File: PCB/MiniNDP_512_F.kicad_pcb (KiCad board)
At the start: 2 copper layers, 60 x 34 mm, 19 parts, among them J1 Conn_02x20_Odd_Even, U1 HC238, U2 HC4040, U3 FCT841, U4 AS6C4008, U5 2G00

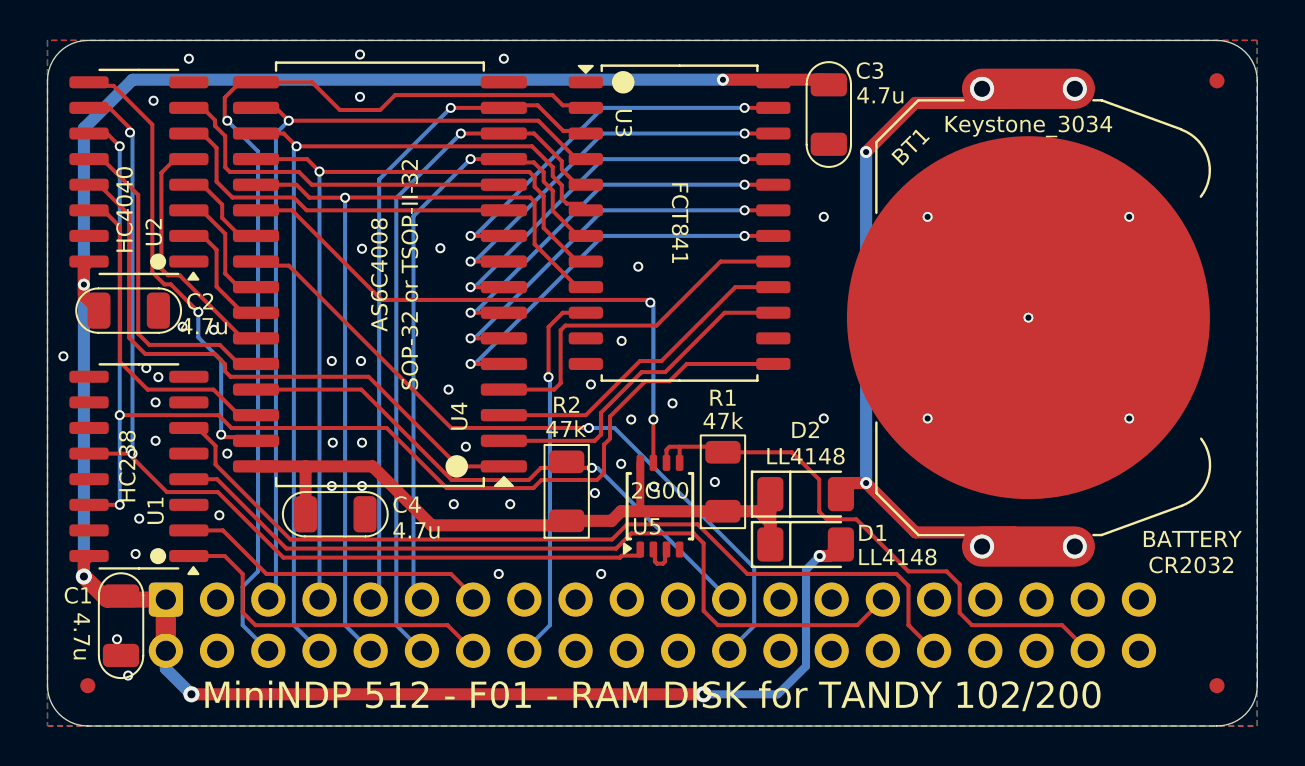
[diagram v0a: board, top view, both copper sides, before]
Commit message: replace 512_F with 512_G
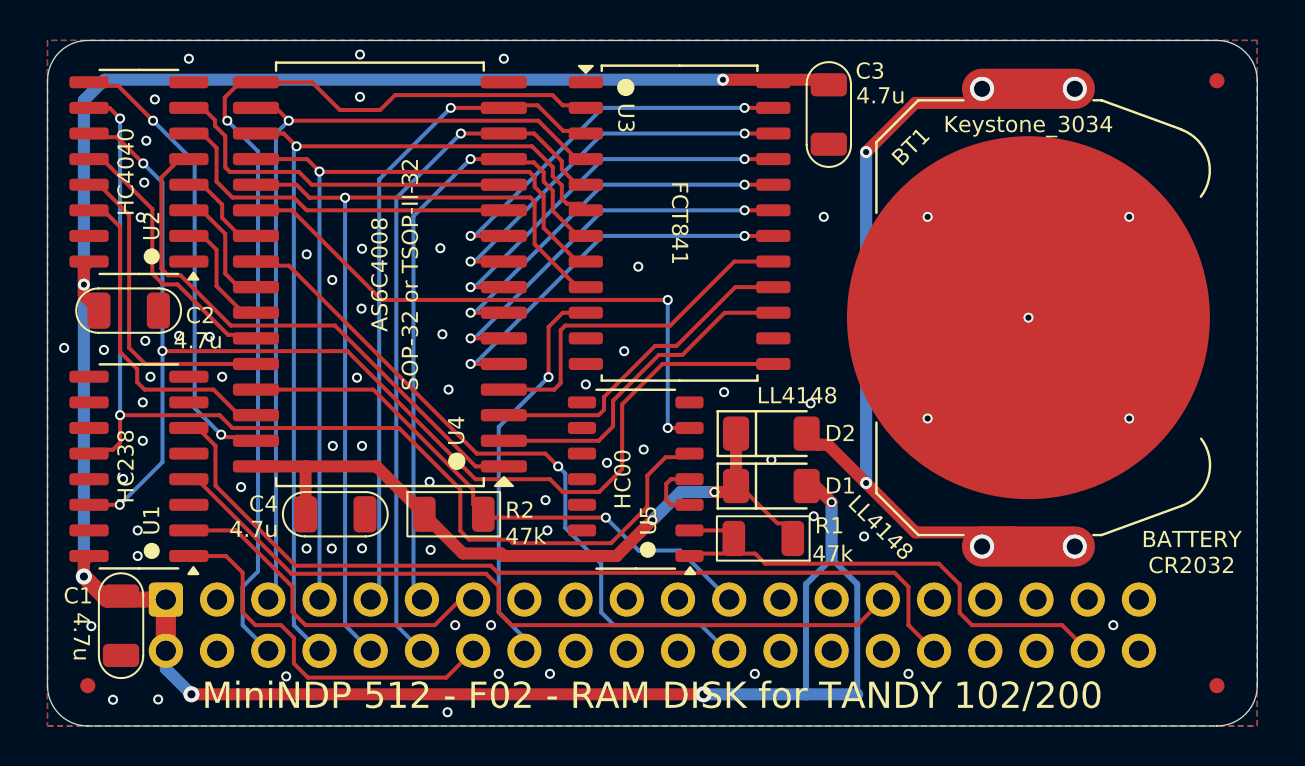
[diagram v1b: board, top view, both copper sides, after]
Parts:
- U5: value 2G00 -> HC00; footprint 000_LOCAL:TSSOP-8_3x3mm_P0.65mm -> 000_LOCAL:SOIC-14_3.9x8.7mm_P1.27mm
- moved R2 5.71 mm to (142.1, 109.5), turned to 0 degrees
- moved R1 3.45 mm to (157.4, 110.7), turned to 180 degrees
- moved D2 3.45 mm to (157.8, 105.5)
- moved D1 3.36 mm to (157.8, 108.1)
- moved U5 1.80 mm to (151.1, 107.8), turned to 180 degrees
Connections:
- U4 pad 1: /A7 -> /A3
- U4 pad 27: /A3 -> /A8
- U4 pad 28: /A8 -> /A7
- U5 pad 1: /BYTE -> /RAMRST
- U5 pad 2: Net-(U5-Pad2) -> /RAMRST
- U5 pad 3: Net-(U5-Pad2) -> Net-(U5-Pad3)
- U5 pad 4: GND -> Net-(U5-Pad3)
- U5 pad 5: /RAMRST -> /BYTE
- U5 pad 6: /RAMRST -> /~{CE}
- U5 pad 7: /~{CE} -> GND
- U5 pad 8: VMEM -> unconnected-(U5-Pad8)
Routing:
- net /A3: track 12.5 -> 27.3 mm
- net VBUS: track 112.1 -> 126.7 mm
- net /A7: track 30.1 -> 15.8 mm
- net /BYTE: track 48.6 -> 54.4 mm
- net Net-(U5-Pad3): track 0.00 -> 3.31 mm
- net /A8: track 16.5 -> 13.8 mm
- net /RAMRST: track 28.4 -> 25.7 mm
- net +BATT: track 36.6 -> 39.1 mm
- net /BUS_A8: track 17.2 -> 19.0 mm
- net Net-(U5-Pad2): track 1.84 -> 0.00 mm
- net /~{Y0}: track 40.5 -> 38.7 mm
- net /BLOCK: track 59.0 -> 60.7 mm
- net /BUS_A9: track 15.6 -> 17.3 mm
- net /~{RD}: track 35.6 -> 34.5 mm
- net /BUS_A10: track 18.8 -> 19.7 mm
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
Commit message: 512-F re-add ramrst diode, both-F remove /WR pullup
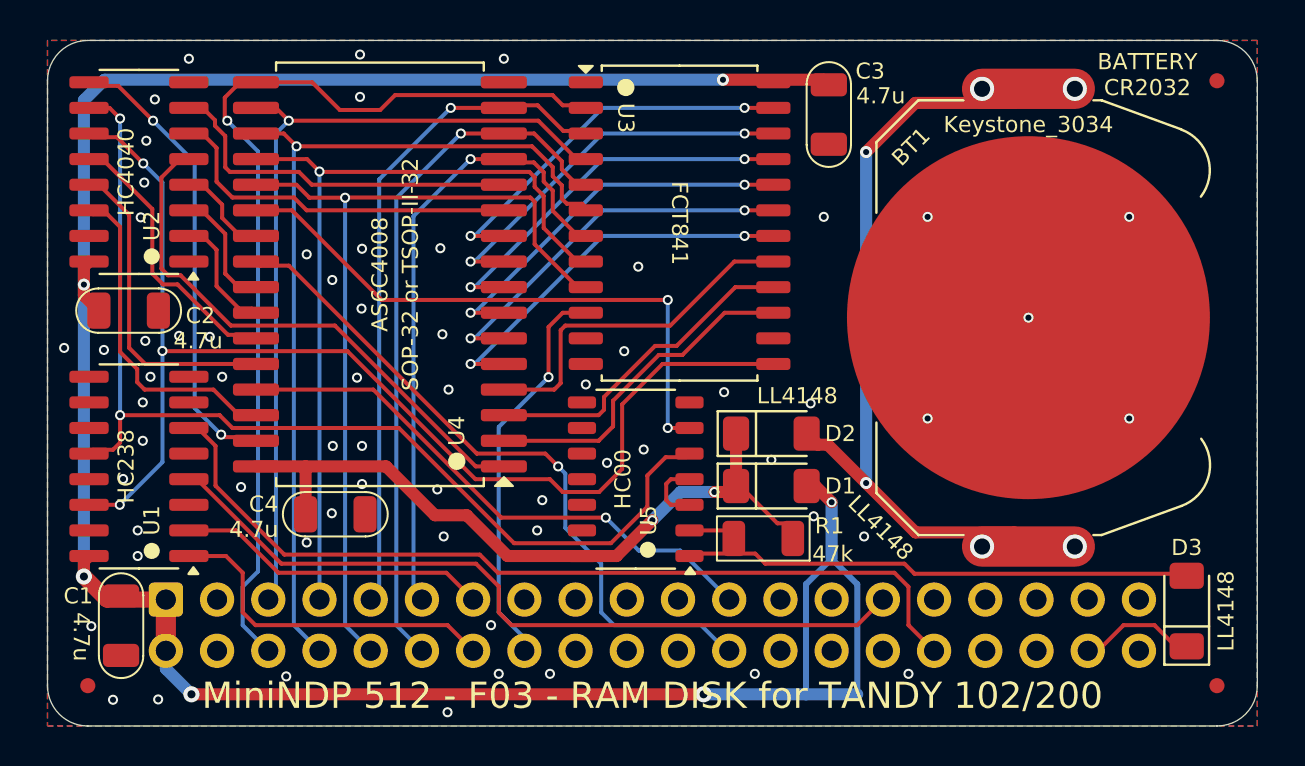
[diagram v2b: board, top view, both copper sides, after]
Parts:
- removed R2: 47k, 000_LOCAL:R_1206
- added D3: LL4148, 000_LOCAL:D_MiniMELF, F.Cu at (178.4, 114.3)
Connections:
- R1 pad 2: /RAMRST -> /SLEEP
- U5 pad 1: /RAMRST -> /SLEEP
- U5 pad 2: /RAMRST -> /SLEEP
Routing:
- net /SLEEP: track 0.00 -> 28.3 mm
- net /RAMRST: track 25.7 -> 5.87 mm
- net /BUS_A8: track 19.0 -> 17.2 mm
- net /BUS_A9: track 17.3 -> 15.5 mm
- net /BYTE: track 54.4 -> 53.2 mm
- net GND: vias 66 -> 64

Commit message: 512_F 1M_C remove ramrst diode, 1u caps
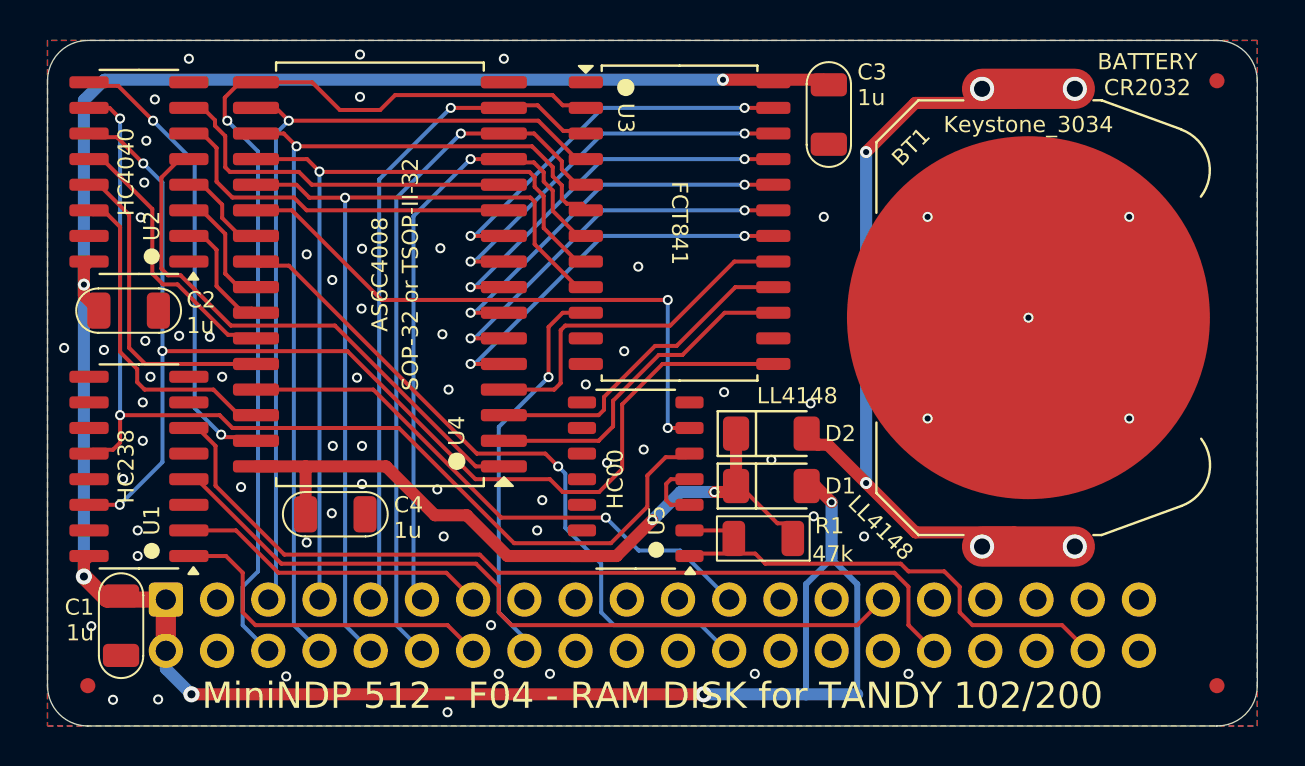
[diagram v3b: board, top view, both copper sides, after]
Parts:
- removed D3: LL4148, 000_LOCAL:D_MiniMELF
- C1, C2, C3, C4: value 4.7u -> 1u
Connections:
- R1 pad 2: /SLEEP -> /RAMRST
- U5 pad 1: /SLEEP -> /RAMRST
- U5 pad 2: /SLEEP -> /RAMRST
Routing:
- net /SLEEP: track 28.3 -> 0.00 mm
- net /RAMRST: track 5.87 -> 25.7 mm

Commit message: easy boards add 47u cap, remove ramrst diode
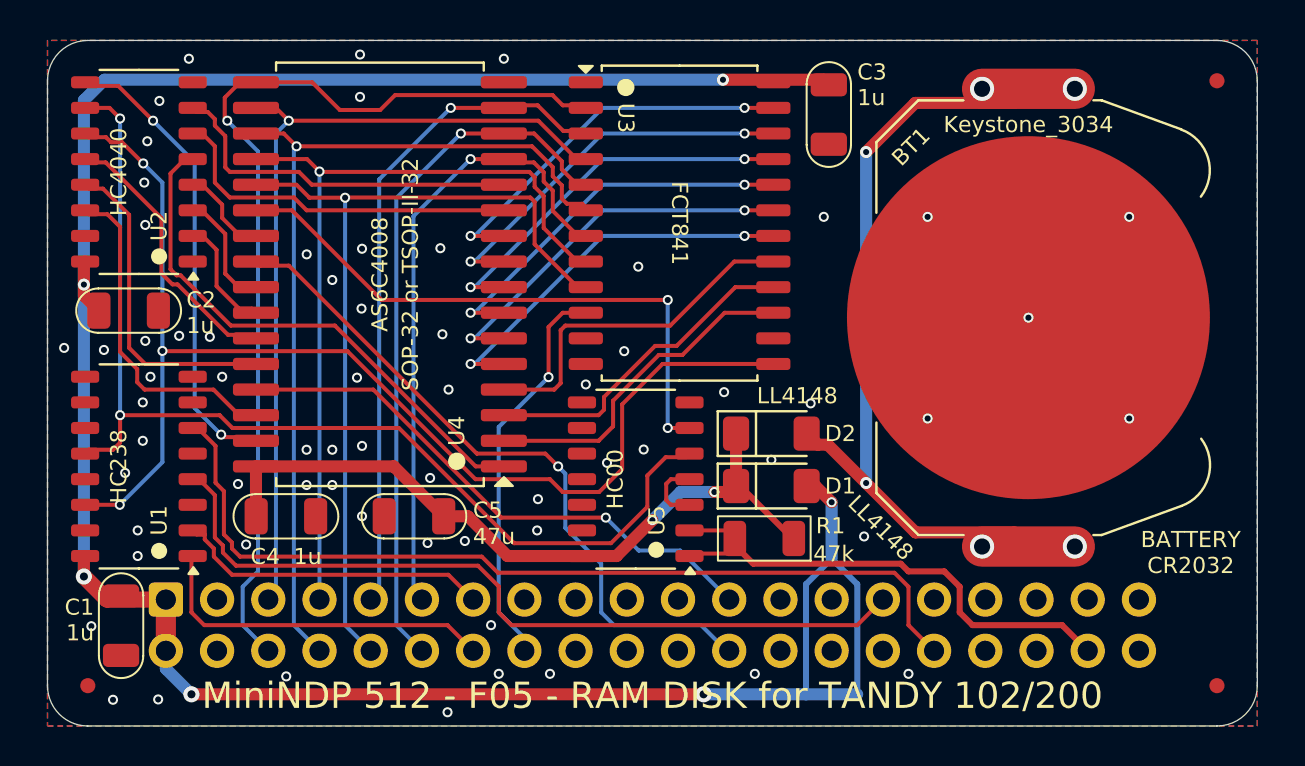
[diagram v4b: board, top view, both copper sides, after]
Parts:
- added C5: 47u, 000_LOCAL:C_1206, F.Cu at (140.1, 109.6)
- moved C4 2.45 mm to (133.8, 109.6)
- moved R1 0.05 mm to (157.5, 110.7)
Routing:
- net /~{Y0}: track 38.7 -> 39.9 mm
- net /(A): track 43.8 -> 45.0 mm
- net /A3: track 27.3 -> 26.7 mm
- net /RAMRST: track 25.7 -> 26.2 mm
- net GND: vias 64 -> 66

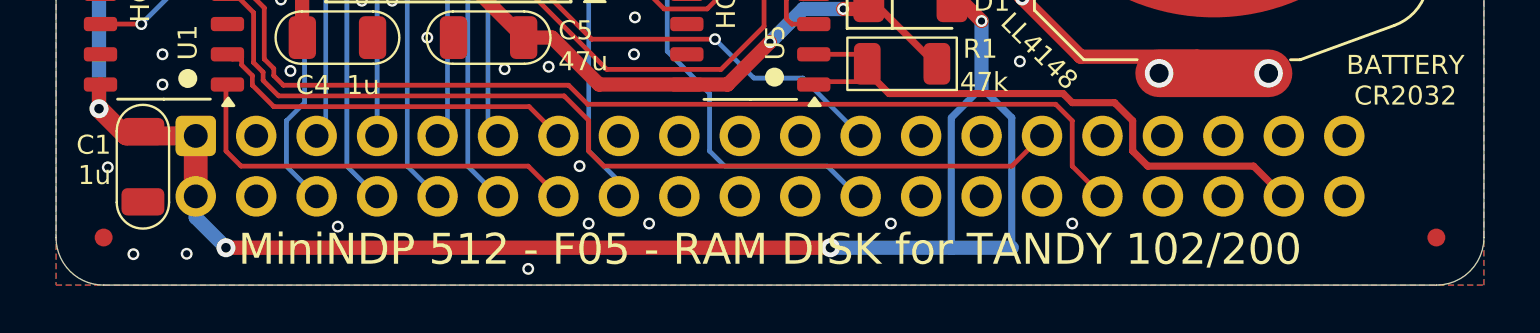
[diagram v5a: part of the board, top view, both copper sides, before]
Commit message: bundle code font
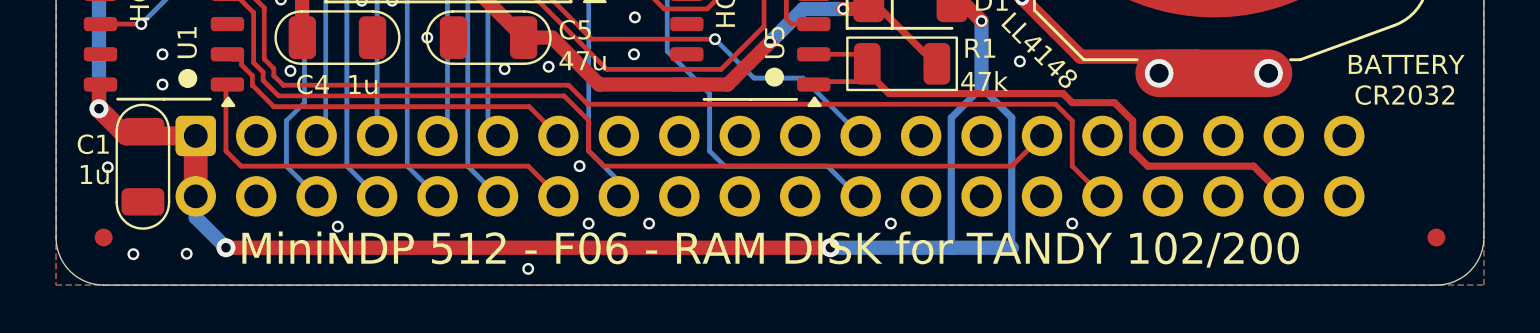
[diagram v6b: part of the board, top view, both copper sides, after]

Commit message: update pcb models for cover
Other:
- board text added: "Install the font from the font directory for the BASIC code below."
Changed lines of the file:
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@@
+		)
+	)
+	(gr_text "Install the font from the font\ndirectory for the BASIC code below.\n"
+		(at 151.95 80.025 0)
+		(layer "Cmts.User")
+		(effects
+			(font
+				(size 2 2)
+				(thickness 0.2)
+			)
+			(justify bottom mirror)
 		)
 	)
 	(gr_text "Use ENIG copper finish\nfor gold plated battery terminal"
 		(at 170.6 84.025 0)
-		(layer "Dwgs.User")
+		(layer "Cmts.User")
 		(effects
 			(font

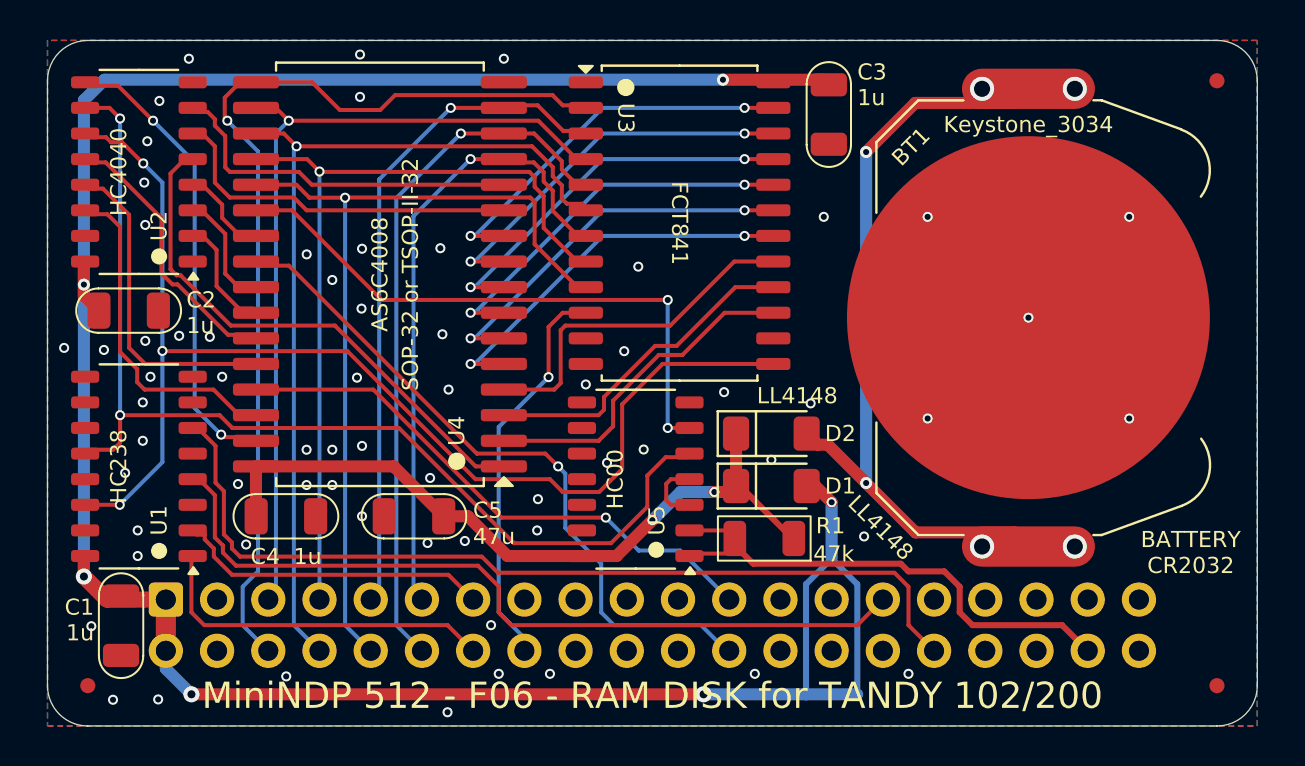
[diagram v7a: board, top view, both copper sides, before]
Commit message: 1M_C move passives around
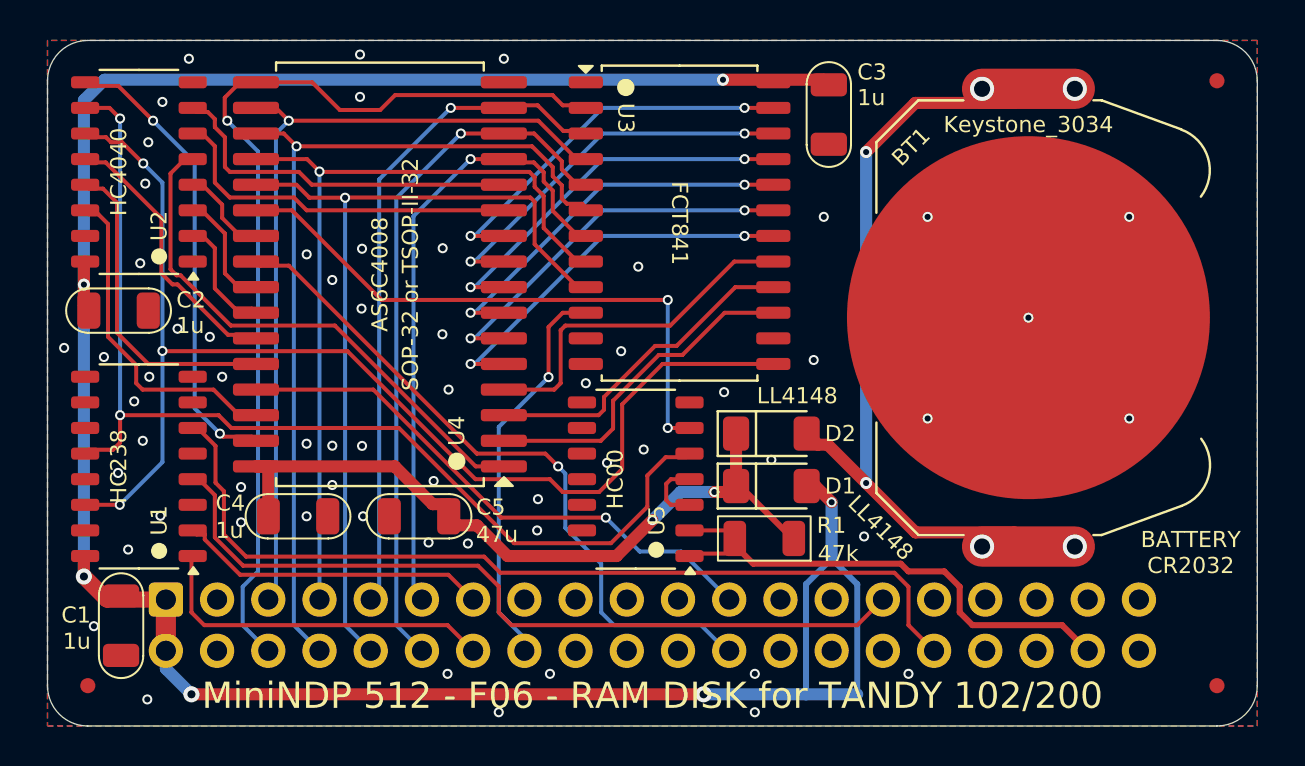
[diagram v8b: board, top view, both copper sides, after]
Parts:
- moved C4 0.60 mm to (134.4, 109.6)
- moved C2 0.50 mm to (125.5, 99.4)
- moved C5 0.25 mm to (140.4, 109.6)
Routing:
- net VMEM: track 36.1 -> 37.1 mm
- net GND: vias 66 -> 62
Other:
- board text added: "Install the font in the font directory for the BASIC code."
- board text added: "Use ENIG copper finish for gold battery terminal."
- board text removed: "Install the font from the font directory for the BASIC code below."
- board text removed: "Use ENIG copper finish for gold plated battery terminal"
